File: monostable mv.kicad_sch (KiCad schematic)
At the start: 5 parts

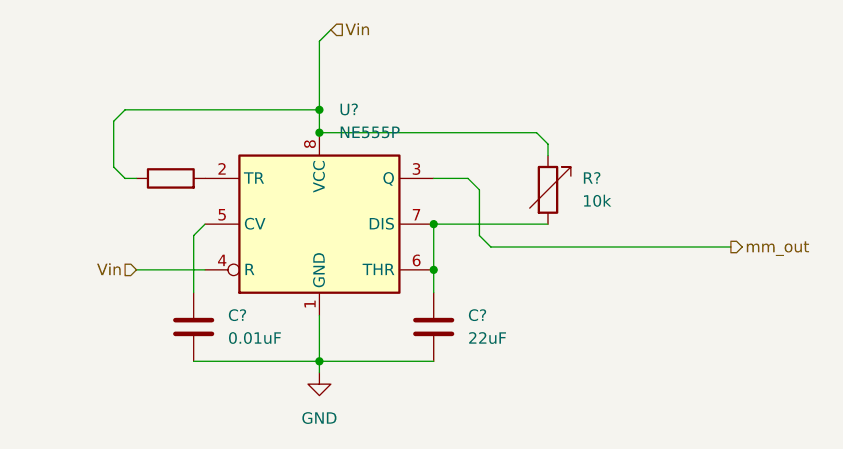
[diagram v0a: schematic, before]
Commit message: added Multipage Schematics
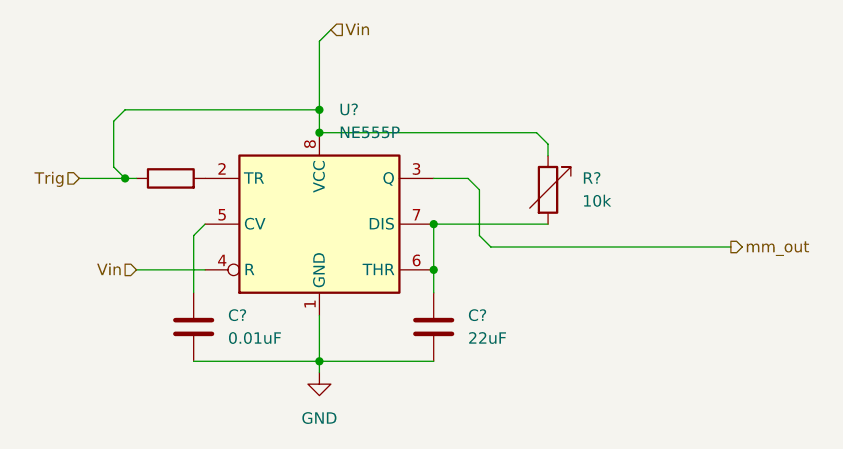
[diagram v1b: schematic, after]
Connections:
- net Vin renamed Trig
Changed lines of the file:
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@@
+	)
+	(junction
+		(at 100.33 100.33)
+		(diameter 0)
+		(color 0 0 0 0)
 	)
 	(junction
@@
 		(pts
 			(xy 121.92 120.65) (xy 134.62 120.65)
+		)
+		(stroke
+			(width 0)
+			(type default)
+		)
+	)
+	(wire
+		(pts
+			(xy 95.25 100.33) (xy 100.33 100.33)
 		)
 		(stroke
@@
 		(fields_autoplaced yes)
 		(effects
+			(font
+				(size 1.27 1.27)
+			)
+			(justify right)
+		)
+	)
+	(hierarchical_label "Trig"
+		(shape input)
+		(at 95.25 100.33 180)
+		(fields_autoplaced yes)
+		(effects

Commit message: preRelease 0.1.0
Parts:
- C: renamed from C?; value 0.01uF -> 220uF
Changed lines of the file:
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@@
 		(dnp no)
 		(fields_autoplaced yes)
-		(property "Reference" "C?"
+		(property "Reference" "C"
 			(at 111.76 115.5699 0)
 			(effects
@@
 			)
 		)
-		(property "Value" "0.01uF"
+		(property "Value" "220uF"
 			(at 111.76 118.1099 0)
 			(effects
@@
 			(project "TENS Device"
 				(path "/b9aff4a0-d82a-4bce-ac01-704fb6f0f3d4/3344af60-ddea-4236-964a-cf859dc1c1a4"
-					(reference "C?")
+					(reference "C")
 					(unit 1)
 				)

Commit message: update
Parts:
- C: renamed from C?; value 22uF -> 220uF
- C_1: renamed from C; value 220uF -> 0.01uF
- R_sw: renamed from Rref?; value 1k -> 470
- gave numbers to parts that had none: 1
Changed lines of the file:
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@@
+	(wire
+		(pts
+			(xy 140.97 107.95) (xy 144.78 107.95)
+		)
+		(stroke
+			(width 0)
+			(type default)
+		)
+	)
 	(wire
 		(pts
@@
 		(pts
 			(xy 147.32 96.52) (xy 147.32 97.79)
-		)
-		(stroke
-			(width 0)
-			(type default)
-		)
-	)
-	(wire
-		(pts
-			(xy 140.97 107.95) (xy 167.64 107.95)
 		)
 		(stroke
@@
 	(hierarchical_label "mm_out"
 		(shape output)
-		(at 167.64 107.95 0)
+		(at 144.78 107.95 0)
 		(fields_autoplaced yes)
 		(effects
@@
 		(on_board yes)
 		(dnp no)
-		(fields_autoplaced yes)
-		(property "Reference" "C?"
-			(at 138.43 115.5699 0)
-			(effects
-				(font
-					(size 1.27 1.27)
-				)
-				(justify left)
-			)
-		)
-		(property "Value" "22uF"
-			(at 138.43 118.1099 0)
+		(property "Reference" "C"
+			(at 135.89 114.046 0)
+			(effects
+				(font
+					(size 1.27 1.27)
+				)
+				(justify left)
+			)
+		)
+		(property "Value" "220uF"
+			(at 130.81 119.888 90)
 			(effects
 				(font
@@
 			(project "TENS Device"
 				(path "/b9aff4a0-d82a-4bce-ac01-704fb6f0f3d4/3344af60-ddea-4236-964a-cf859dc1c1a4"
-					(reference "C?")
+					(reference "C")
 					(unit 1)
 				)
@@
 		(dnp no)
 		(fields_autoplaced yes)
-		(property "Reference" "R?"
+		(property "Reference" "R_pot"
 			(at 151.13 100.3299 0)
 			(effects
@@
 			(project "TENS Device"
 				(path "/b9aff4a0-d82a-4bce-ac01-704fb6f0f3d4/3344af60-ddea-4236-964a-cf859dc1c1a4"
-					(reference "R?")
+					(reference "R_pot")
 					(unit 1)
 				)
@@
 		(on_board yes)
 		(dnp no)
-		(fields_autoplaced yes)
-		(property "Reference" "Rref?"
-			(at 104.1399 97.79 0)
-			(effects
-				(font
-					(size 1.27 1.27)
-				)
-				(justify left)
-				(hide yes)
-			)
-		)
-		(property "Value" "1k"
-			(at 106.6799 97.79 0)
-			(effects
-				(font
-					(size 1.27 1.27)
-				)
-				(justify left)
-				(hide yes)
+		(property "Reference" "R_sw"
+			(at 107.442 98.044 90)
+			(effects
+				(font
+					(size 1.27 1.27)
+				)
+				(justify left)
+			)
+		)
+		(property "Value" "470"
+			(at 106.934 100.33 90)
+			(effects
+				(font
+					(size 1.27 1.27)
+				)
+				(justify left)
 			)
 		)
@@
 			(project "TENS Device"
 				(path "/b9aff4a0-d82a-4bce-ac01-704fb6f0f3d4/3344af60-ddea-4236-964a-cf859dc1c1a4"
-					(reference "Rref?")
+					(reference "R_sw")
 					(unit 1)
 				)
@@
 		(dnp no)
 		(fields_autoplaced yes)
-		(property "Reference" "C"
+		(property "Reference" "C_1"
 			(at 111.76 115.5699 0)
 			(effects
@@
 			)
 		)
-		(property "Value" "220uF"
+		(property "Value" "0.01uF"
 			(at 111.76 118.1099 0)
 			(effects
@@
 			(project "TENS Device"
 				(path "/b9aff4a0-d82a-4bce-ac01-704fb6f0f3d4/3344af60-ddea-4236-964a-cf859dc1c1a4"
-					(reference "C")
+					(reference "C_1")
 					(unit 1)
 				)
